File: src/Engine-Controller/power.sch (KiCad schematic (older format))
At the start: 30 parts, among them P1 EJ508A, U2 LM22672MRE-5.0_NOPB, U3 LMS8117AMP-3.3_NOPB, U6 TPS2115APWR

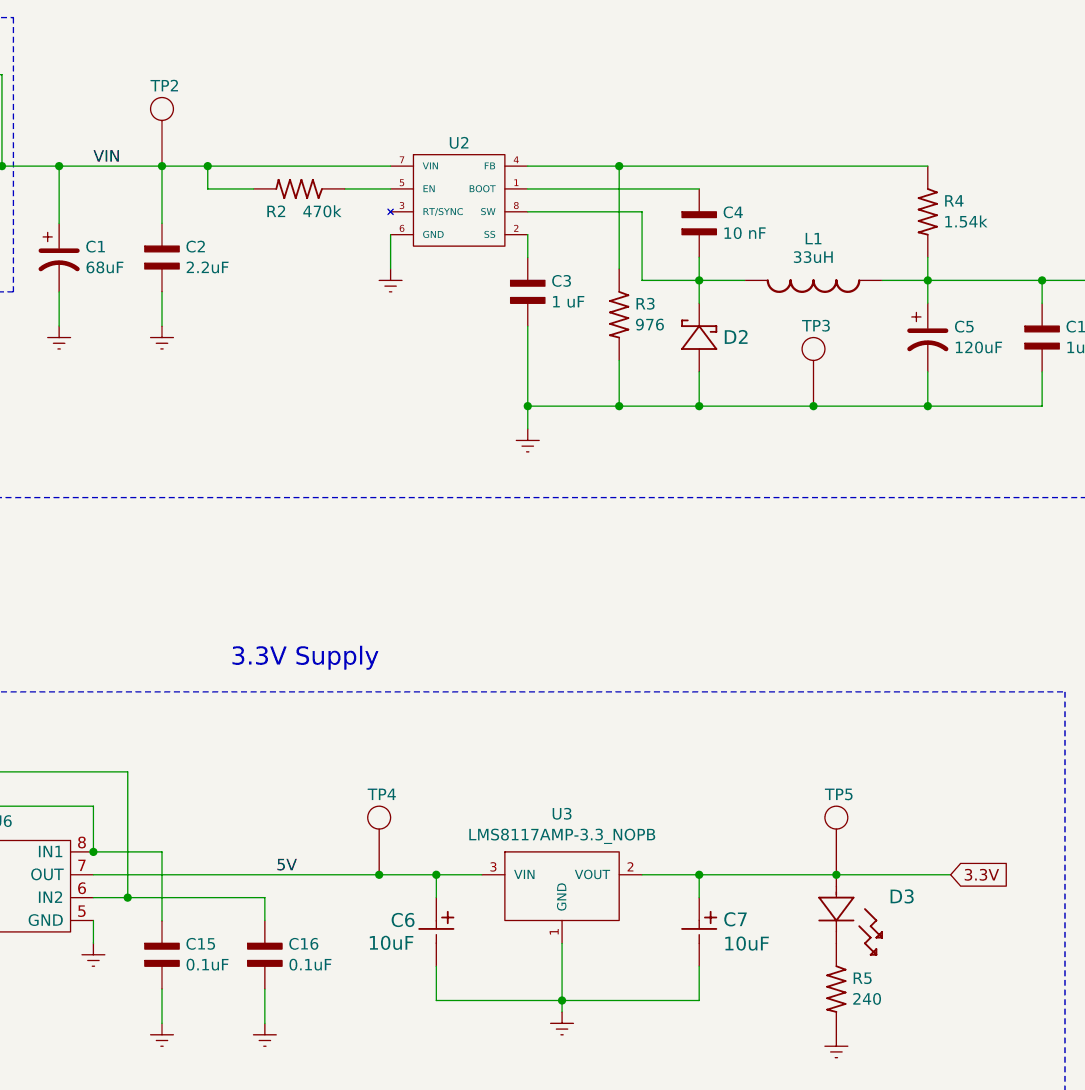
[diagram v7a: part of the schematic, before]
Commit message: Added polarity marking to C1
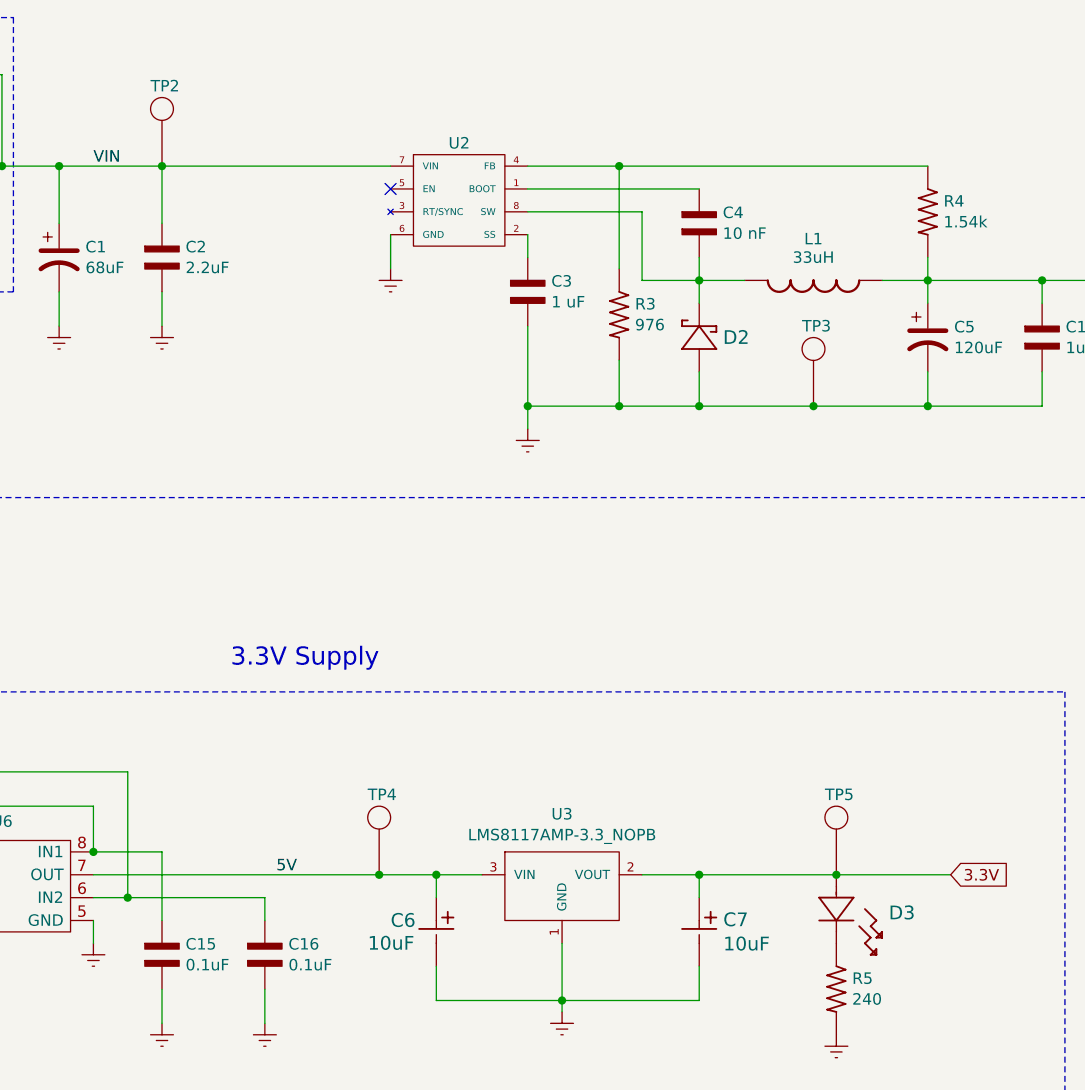
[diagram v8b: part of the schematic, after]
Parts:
- removed D3: LTST-C150GKT, Engine-Controller:LTST-C150GKT, symbol Engine-Controller:LTST-C150GKT
- removed R2: 470k, Engine-Controller:RES_0805, symbol Engine-Controller:RES_0805
- added D3: SML-LX1206GC-TR, symbol Engine-Controller:SML-LX1206GC-TR
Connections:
- net 3.3V: now also D3.2
- net at R5.1: now also D3.1
- no-connect marks 1 -> 2
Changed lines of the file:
@@
 $EndDescr
-$Comp
-L Engine-Controller:LTST-C150GKT D3
-U 1 1 60EB9E6E
-P 7600 5450
-F 0 "D3" H 7829 5553 60  0000 L CNN
-F 1 "LTST-C150GKT" H 7829 5447 60  0001 L CNN
-F 2 "Engine-Controller:LTST-C150GKT" H 7800 5090 60  0001 C CNN
-F 3 "" V 7600 5700 60  0000 C CNN
-	1    7600 5450
-	1    0    0    -1
-$EndComp
 $Comp
 L Engine-Controller:CBC3225T220KR L1
@@
 	4650 2400 4650 2150
 $Comp
-L Engine-Controller:RES_0805 R2
-U 1 1 60EEF47A
-P 5250 2250
-F 0 "R2" H 5350 2350 50  0000 C CNN
-F 1 "470k" H 5150 2350 50  0000 C CNN
-F 2 "Engine-Controller:RES_0805" H 5300 1750 50  0001 L BNN
-F 3 "" H 5250 2250 50  0001 L BNN
-	1    5250 2250
-	-1   0    0    1
-$EndComp
-$Comp
 L Engine-Controller:CAP_0603 C3
 U 1 1 60EF8CF7
@@
 $EndComp
 Wire Wire Line
-	4850 2250 4850 2150
-Wire Wire Line
 	6250 2450 6250 2550
 $Comp
@@
 Connection ~ 4650 2150
 Wire Wire Line
-	4650 2150 4850 2150
-Wire Wire Line
 	5650 2450 5650 2600
 $Comp
@@
 $EndComp
 Wire Wire Line
-	5650 2150 4850 2150
-Connection ~ 4850 2150
-Wire Wire Line
 	6750 2350 6750 2650
 Wire Wire Line
@@
 Wire Wire Line
 	8000 2150 6650 2150
-Wire Wire Line
-	4850 2250 5050 2250
-Wire Wire Line
-	5450 2250 5650 2250
 $Comp
 L Engine-Controller:RES_0603 R3
@@
 Wire Wire Line
 	8500 2650 8750 2650
+$Comp
+L Engine-Controller:SML-LX1206GC-TR D3
+U 1 1 614BA3CC
+P 7600 5450
+F 0 "D3" H 7829 5483 60  0000 L CNN
+F 1 "SML-LX1206GC-TR" H 7829 5430 60  0001 L CNN
+F 2 "" H 7800 5090 60  0001 C CNN
+F 3 "" V 7600 5700 60  0000 C CNN
+	1    7600 5450
+	1    0    0    -1
+$EndComp
+Wire Wire Line
+	4650 2150 5650 2150
+NoConn ~ 5650 2250
 $EndSCHEMATC
